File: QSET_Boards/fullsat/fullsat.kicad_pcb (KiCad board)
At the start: 4 copper layers, 82 x 325.9 mm, 26 parts

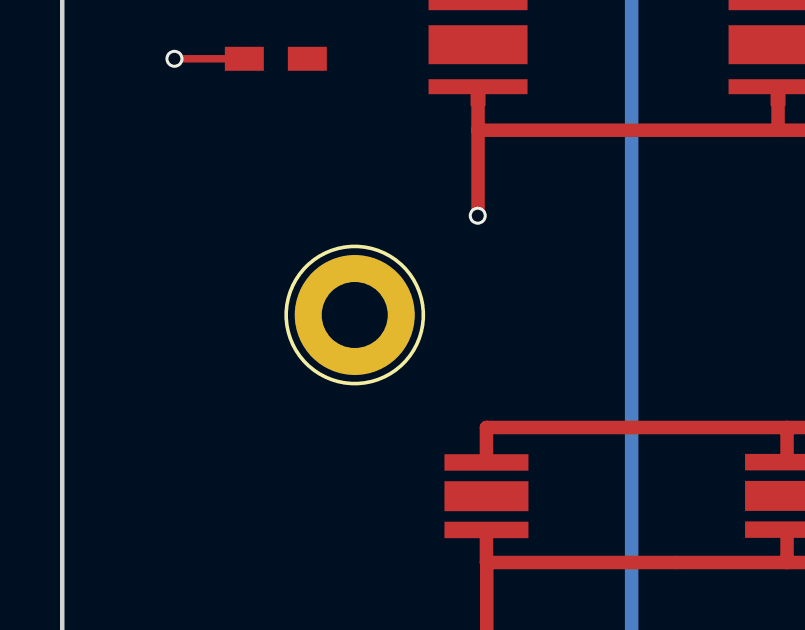
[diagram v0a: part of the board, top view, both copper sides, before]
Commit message: add buzzer footprint
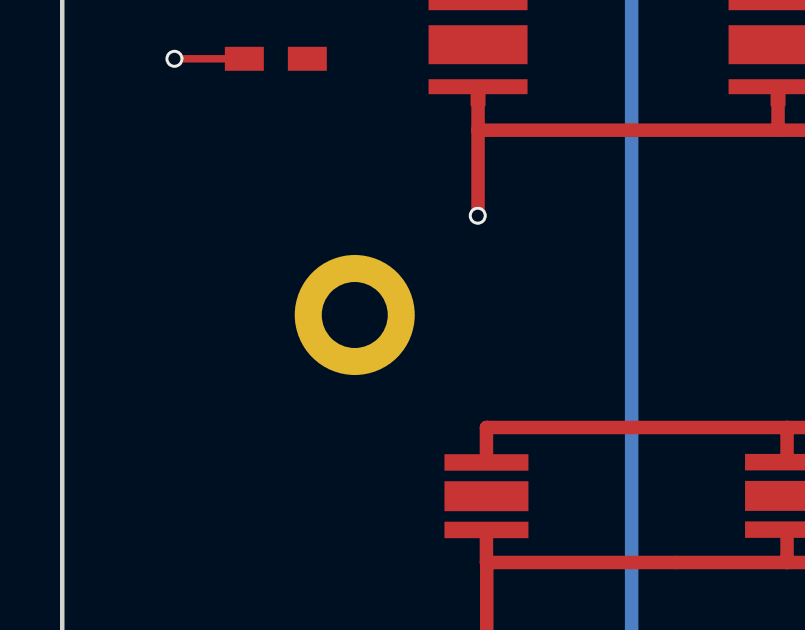
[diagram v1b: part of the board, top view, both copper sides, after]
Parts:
- ?: moved to B.Cu
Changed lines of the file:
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@@
-(kicad_pcb (version 4) (host pcbnew 4.0.7-e2-6376~58~ubuntu16.04.1)
+(kicad_pcb (version 20171130) (host pcbnew "(5.0.1)-3")
   (general
-    (links 0)
-    (no_connects 0)
-    (area 58.464999 19.907 140.615001 347.905)
     (thickness 1.6)
     (drawings 34)
@@
   (layers
     (0 F.Cu power)
-    (1 In1.Cu signal)
-    (2 In2.Cu signal)
-    (31 B.Cu signal)
+    (1 In1.Cu signal hide)
+    (2 In2.Cu signal hide)
+    (31 B.Cu signal hide)
     (32 B.Adhes user)
     (33 F.Adhes user)
@@
     (pad_drill 2.2)
     (pad_to_mask_clearance 0.2)
+    (solder_mask_min_width 0.25)
     (aux_axis_origin 0 0)
     (visible_elements 7FFFFFFF)
@@
       (layerselection 0x010f0_80000007)
       (usegerberextensions false)
+      (usegerberattributes false)
+      (usegerberadvancedattributes false)
+      (creategerberjobfile false)
       (excludeedgelayer true)
       (linewidth 0.100000)
@@
       (hpglpennumber 1)
       (hpglpenspeed 20)
-      (hpglpendiameter 15)
-      (hpglpenoverlay 2)
+      (hpglpendiameter 15.000000)
       (psnegative false)
       (psa4output false)
@@
       (drillshape 0)
       (scaleselection 1)
-      (outputdirectory pdfs/))
+      (outputdirectory "pdfs/"))
   )
   (net 0 "")
@@
     (pad 1 thru_hole circle (at 0 0) (size 4 4) (drill 2.2) (layers *.Cu *.Mask))
   )
-  (module Connectors:1pin (layer F.Cu)
+  (module Connectors:1pin (layer B.Cu)
     (at 68.29 137.63)
     (descr "module 1 pin (ou trou mecanique de percage)")
     (tags DEV)
-    (fp_text reference "" (at 0 -3.048) (layer F.SilkS)
-      (effects (font (size 1 1) (thickness 0.15)))
-    )
-    (fp_text value "" (at 0 3) (layer F.Fab)
-      (effects (font (size 1 1) (thickness 0.15)))
-    )
-    (fp_circle (center 0 0) (end 2 0.8) (layer F.Fab) (width 0.1))
-    (fp_circle (center 0 0) (end 2.6 0) (layer F.CrtYd) (width 0.05))
-    (fp_circle (center 0 0) (end 0 -2.286) (layer F.SilkS) (width 0.12))
-    (pad 1 thru_hole circle (at 0 0) (size 4 4) (drill 2.2) (layers *.Cu *.Mask))
-  )
+    (fp_text reference "" (at 0 3.048) (layer B.SilkS)
+      (effects (font (size 1 1) (thickness 0.15)) (justify mirror))
+    )
+    (fp_text value "" (at 0 -3) (layer B.Fab)
+      (effects (font (size 1 1) (thickness 0.15)) (justify mirror))
+    )
+    (fp_circle (center 0 0) (end 2 -0.8) (layer B.Fab) (width 0.1))
+    (fp_circle (center 0 0) (end 2.6 0) (layer B.CrtYd) (width 0.05))
+    (fp_circle (center 0 0) (end 0 2.286) (layer B.SilkS) (width 0.12))
+    (pad 1 thru_hole circle (at 0 0) (size 4 4) (drill 2.2) (layers *.Cu *.Mask))
+  )
